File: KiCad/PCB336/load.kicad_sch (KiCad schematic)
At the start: 37 parts, among them IC8 ADUM3195BRQZ, J4 MOLEX_172298-1108, K1 32.21.7.024.4000, K2 32.21.7.024.4000, K3 32.21.7.024.4000, K4 32.21.7.024.4000, Q10 2N7002LT1G, Q11 2N7002LT1G, Q8 2N7002LT1G, Q9 2N7002LT1G, U4 TME-0505S

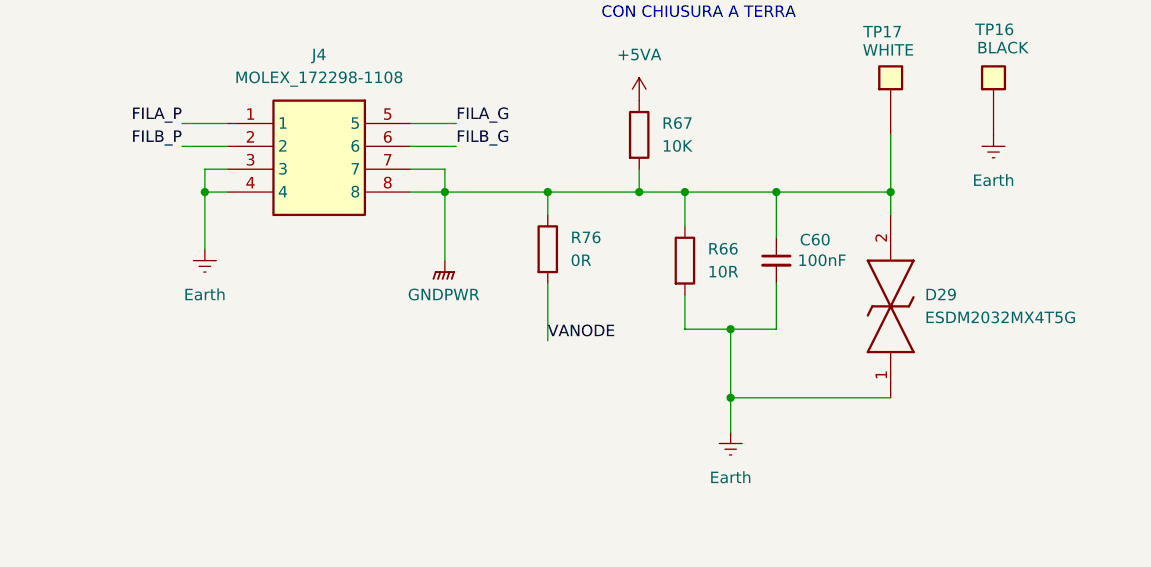
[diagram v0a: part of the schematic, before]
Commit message: Iniziato loi sbroglio
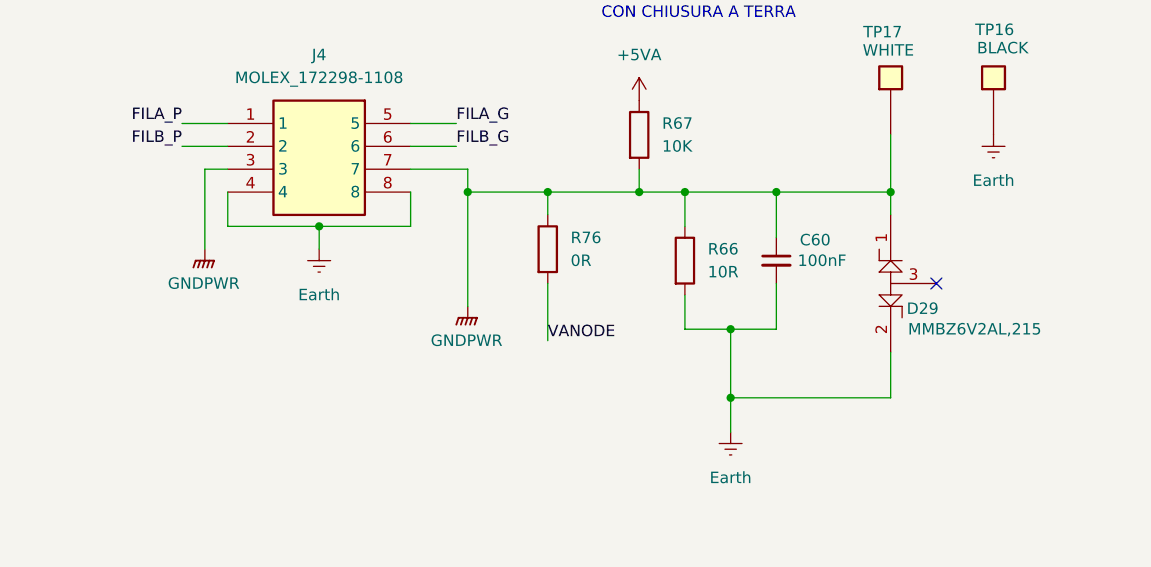
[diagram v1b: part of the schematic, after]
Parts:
- removed D29: ESDM2032MX4T5G, MET:ESDM2032MX4T5G, symbol MET:ESDM2032MX4T5G
- added D29: MMBZ6V2AL,215, MET:MMBZ6V2AL,215, symbol MET:MMBZ6V2AL,215
- R76: footprint MET:RES_10R_SMW210R -> Resistor_SMD:R_0603_1608Metric_Pad0.98x0.95mm_HandSolder; PN SMW210RJT -> (none)
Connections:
- net Earth: now also J4.8, D29.2 (CATHODE_(DIODE_2)); no longer J4.3
- net GNDPWR: now also J4.3, D29.1 (CATHODE_(DIODE_1)); no longer J4.8
- no-connect marks 0 -> 1
